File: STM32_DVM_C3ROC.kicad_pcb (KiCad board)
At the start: 4 copper layers, 65 x 56 mm, 18 parts, among them J3 40HAT, J6 CONN_02X02, J9 CONN_01X02, Q1 DMG2305UX, Q2 DMMT5401, U2 CAT24C32

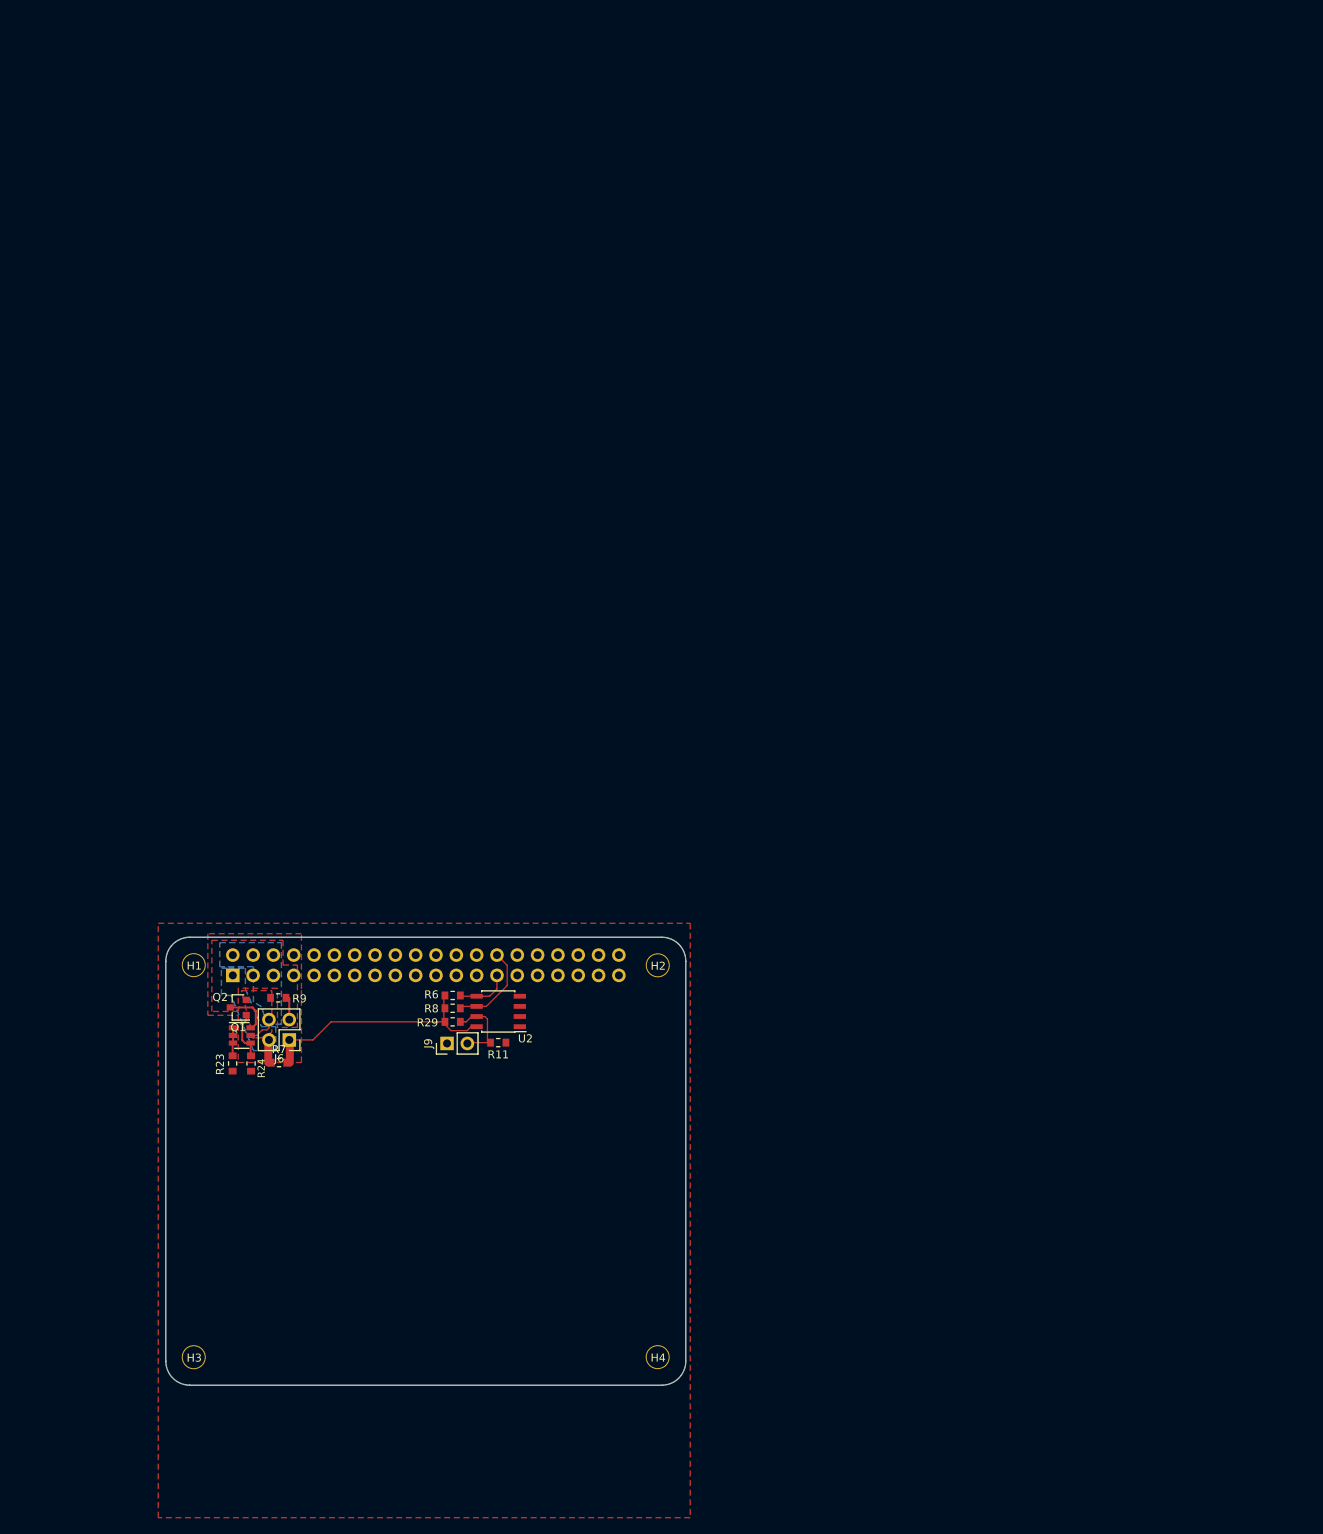
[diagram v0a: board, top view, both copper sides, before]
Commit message: Schaltplan fertig, Footprints zugewiesen, PCB Beginn platzierung
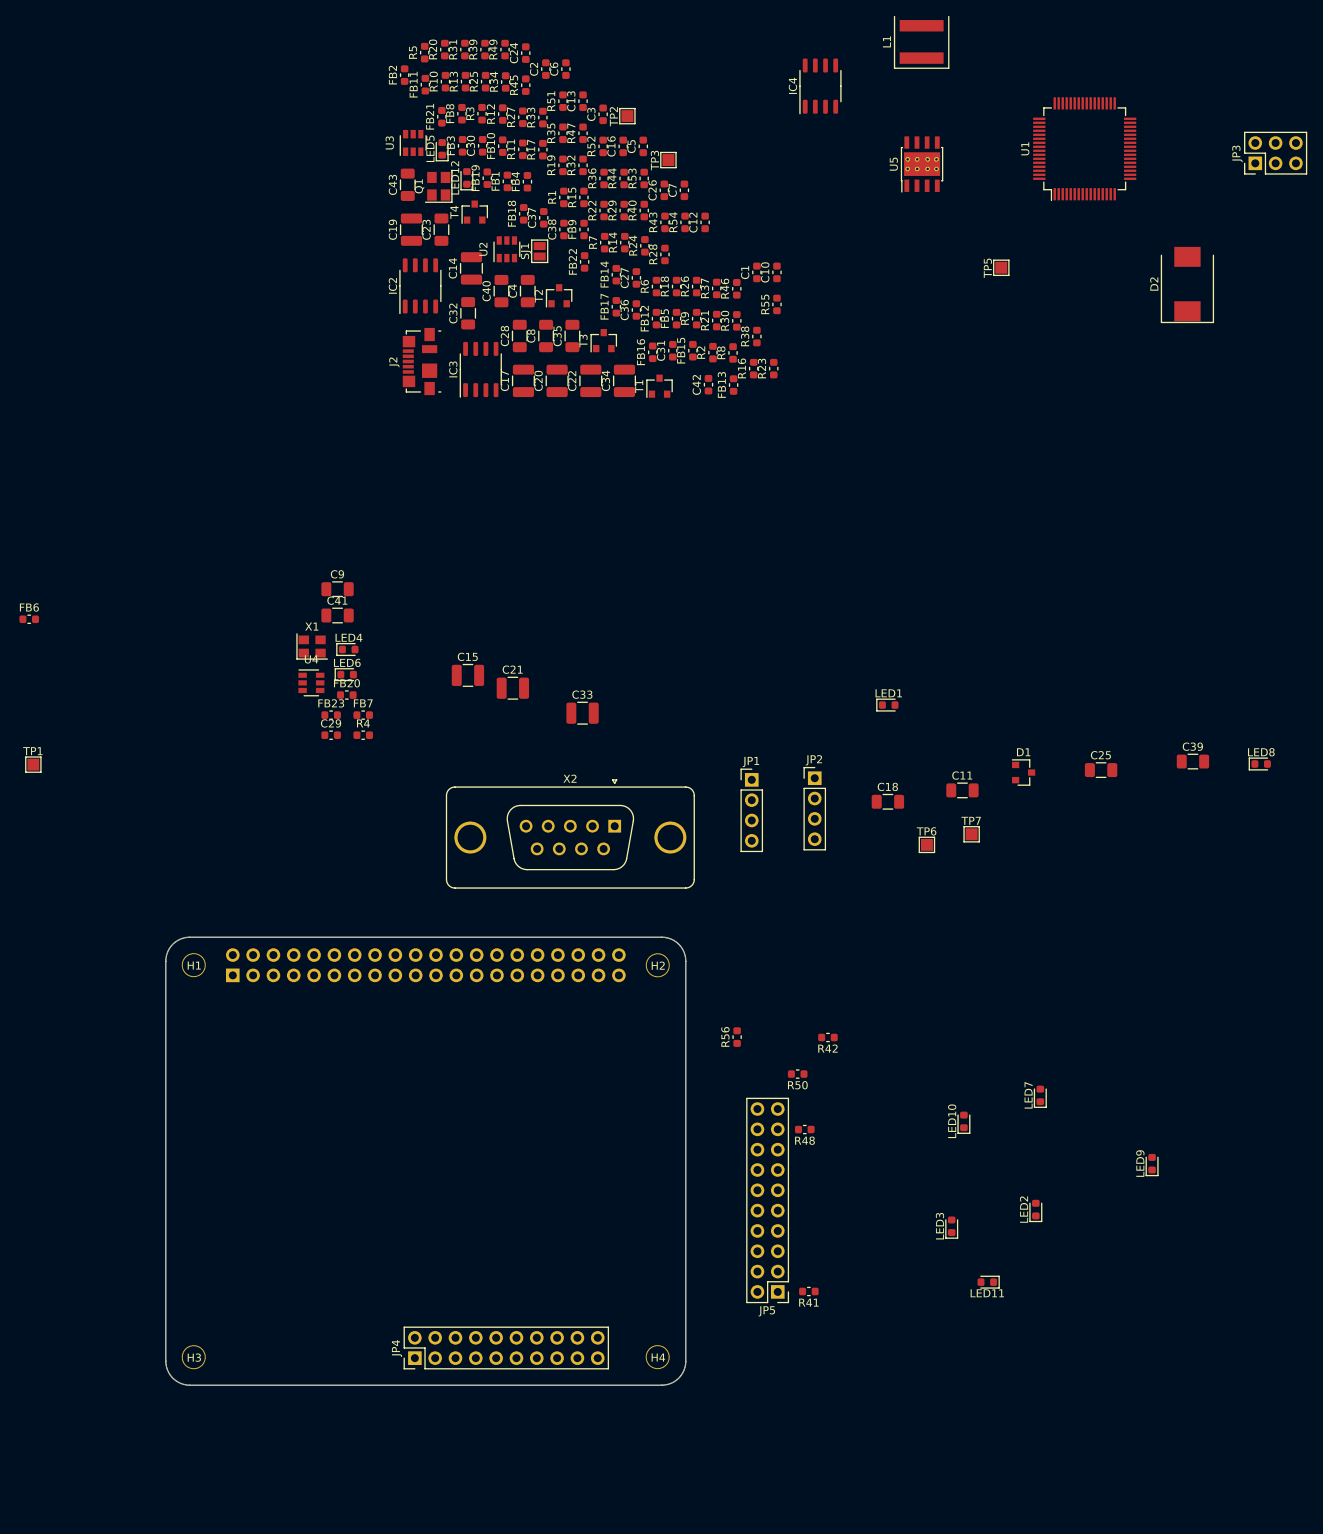
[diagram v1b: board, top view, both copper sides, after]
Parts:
- removed J6: CONN_02X02, Connector_PinHeader_2.54mm:PinHeader_2x02_P2.54mm_Vertical
- removed J9: CONN_01X02, Connector_PinHeader_2.54mm:PinHeader_1x02_P2.54mm_Vertical
- removed Q2: DMMT5401, Package_TO_SOT_SMD:SOT-23-6
- added C1: 100n, Capacitor_SMD:C_0603_1608Metric, F.Cu at (152.4, -22.3)
- added C10: 100n, Capacitor_SMD:C_0603_1608Metric, F.Cu at (154.9, -22.3)
- added C11: 4u7, Capacitor_SMD:C_1206_3216Metric, F.Cu at (178.1, 42.5)
- added C12: 10p, Capacitor_SMD:C_0603_1608Metric, F.Cu at (146.0, -28.5)
- added C13: 10p, Capacitor_SMD:C_0603_1608Metric, F.Cu at (130.7, -43.7)
- added C14: 22u, Capacitor_SMD:C_1210_3225Metric, F.Cu at (116.8, -22.8)
- added C15: 47u, Capacitor_SMD:C_1210_3225Metric, F.Cu at (116.3, 28.1)
- added C16: 100n, Capacitor_SMD:C_0603_1608Metric, F.Cu at (135.7, -38.0)
- added C17: 47u, Capacitor_SMD:C_1210_3225Metric, F.Cu at (123.3, -8.72)
- added C18: 4u7, Capacitor_SMD:C_1206_3216Metric, F.Cu at (168.8, 43.9)
- added C19: 22u, Capacitor_SMD:C_1210_3225Metric, F.Cu at (109.3, -27.6)
- added C2: 100n, Capacitor_SMD:C_0603_1608Metric, F.Cu at (126.1, -47.7)
- added C20: 22u, Capacitor_SMD:C_1210_3225Metric, F.Cu at (127.5, -8.72)
- added C21: 47u, Capacitor_SMD:C_1210_3225Metric, F.Cu at (121.9, 29.7)
- added C22: 47u, Capacitor_SMD:C_1210_3225Metric, F.Cu at (131.7, -8.72)
- added C23: 2u2, Capacitor_SMD:C_1206_3216Metric, F.Cu at (113.0, -27.6)
- added C24: 10n, Capacitor_SMD:C_0603_1608Metric, F.Cu at (123.5, -49.7)
- added C25: 2u2, Capacitor_SMD:C_1206_3216Metric, F.Cu at (195.5, 39.9)
- added C26: 10n, Capacitor_SMD:C_0603_1608Metric, F.Cu at (140.9, -32.5)
- added C27: 10n, Capacitor_SMD:C_0603_1608Metric, F.Cu at (137.4, -21.6)
- added C28: 4u7, Capacitor_SMD:C_1206_3216Metric, F.Cu at (122.8, -14.3)
- added C29: 680p, Capacitor_SMD:C_0603_1608Metric, F.Cu at (99.2, 35.6)
- added C3: 100n, Capacitor_SMD:C_0603_1608Metric, F.Cu at (133.2, -42.0)
- added C30: 10n, Capacitor_SMD:C_0603_1608Metric, F.Cu at (118.2, -38.1)
- added C31: 680p, Capacitor_SMD:C_0603_1608Metric, F.Cu at (141.9, -12.5)
- added C32: 4u7, Capacitor_SMD:C_1206_3216Metric, F.Cu at (116.3, -17.2)
- added C33: 22u, Capacitor_SMD:C_1210_3225Metric, F.Cu at (130.6, 32.8)
- added C34: 22u, Capacitor_SMD:C_1210_3225Metric, F.Cu at (135.9, -8.72)
- added C35: 4u7, Capacitor_SMD:C_1206_3216Metric, F.Cu at (129.4, -14.3)
- added C36: 6n8, Capacitor_SMD:C_0603_1608Metric, F.Cu at (137.4, -17.6)
- added C37: 47p, Capacitor_SMD:C_0603_1608Metric, F.Cu at (125.8, -29.1)
- added C38: 100n, Capacitor_SMD:C_0603_1608Metric, F.Cu at (128.3, -27.6)
- added C39: 22u, Capacitor_SMD:C_1206_3216Metric, F.Cu at (206.9, 38.9)
- added C4: 4u7, Capacitor_SMD:C_1206_3216Metric, F.Cu at (123.8, -19.9)
- added C40: 22u, Capacitor_SMD:C_1206_3216Metric, F.Cu at (120.5, -19.9)
- added C41: 1u, Capacitor_SMD:C_1206_3216Metric, F.Cu at (100.0, 20.6)
- added C42: 10n, Capacitor_SMD:C_0603_1608Metric, F.Cu at (146.4, -8.24)
- added C43: 1u, Capacitor_SMD:C_1206_3216Metric, F.Cu at (108.8, -33.2)
- added C5: 100n, Capacitor_SMD:C_0603_1608Metric, F.Cu at (138.2, -38.0)
- added C6: 100n, Capacitor_SMD:C_0603_1608Metric, F.Cu at (128.6, -47.7)
- added C7: 100n, Capacitor_SMD:C_0603_1608Metric, F.Cu at (143.4, -32.5)
- added C8: 4u7, Capacitor_SMD:C_1206_3216Metric, F.Cu at (126.1, -14.3)
- added C9: 4u7, Capacitor_SMD:C_1206_3216Metric, F.Cu at (100.0, 17.3)
- added D1: BAV70, Package_TO_SOT_SMD:SOT-23, F.Cu at (185.8, 40.2)
- added D2: B560C, Diode_SMD:D_SMC, F.Cu at (206.2, -20.8)
- added FB1: 100, Inductor_SMD:L_0603_1608Metric, F.Cu at (121.2, -33.7)
- added FB10: 100, Inductor_SMD:L_0603_1608Metric, F.Cu at (120.7, -38.1)
- added FB11: 100, Inductor_SMD:L_0603_1608Metric, F.Cu at (111.0, -45.7)
- added FB12: 100, Inductor_SMD:L_0603_1608Metric, F.Cu at (139.9, -16.5)
- added FB13: 100, Inductor_SMD:L_0603_1608Metric, F.Cu at (149.5, -8.20)
- added FB14: 100, Inductor_SMD:L_0603_1608Metric, F.Cu at (134.9, -22.0)
- added FB15: 100, Inductor_SMD:L_0603_1608Metric, F.Cu at (144.4, -12.5)
- added FB16: 100, Inductor_SMD:L_0603_1608Metric, F.Cu at (139.4, -12.3)
- added FB17: 100, Inductor_SMD:L_0603_1608Metric, F.Cu at (134.9, -18.0)
- added FB18: 100, Inductor_SMD:L_0603_1608Metric, F.Cu at (123.3, -29.6)
- added FB19: 100, Inductor_SMD:L_0603_1608Metric, F.Cu at (118.7, -34.1)
- added FB2: 100, Inductor_SMD:L_0603_1608Metric, F.Cu at (108.4, -46.9)
- added FB20: 100, Inductor_SMD:L_0603_1608Metric, F.Cu at (101.2, 30.5)
- added FB21: 100, Inductor_SMD:L_0603_1608Metric, F.Cu at (113.1, -41.7)
- added FB22: 100, Inductor_SMD:L_0603_1608Metric, F.Cu at (130.9, -23.6)
- added FB23: 100, Inductor_SMD:L_0603_1608Metric, F.Cu at (99.2, 33.1)
- added FB3: 100, Inductor_SMD:L_0603_1608Metric, F.Cu at (115.6, -38.1)
- added FB4: 100, Inductor_SMD:L_0603_1608Metric, F.Cu at (123.8, -33.6)
- added FB5: 100, Inductor_SMD:L_0603_1608Metric, F.Cu at (142.4, -16.5)
- added FB6: 100, Inductor_SMD:L_0603_1608Metric, F.Cu at (61.5, 21.1)
- added FB7: 100, Inductor_SMD:L_0603_1608Metric, F.Cu at (103.2, 33.1)
- added FB8: 100, Inductor_SMD:L_0603_1608Metric, F.Cu at (115.6, -42.1)
- added FB9: 100, Inductor_SMD:L_0603_1608Metric, F.Cu at (130.8, -27.6)
- added IC2: MCP6002, Package_SO:SO-8_3.9x4.9mm_P1.27mm, F.Cu at (110.4, -20.6)
- added IC3: MCP6002, Package_SO:SO-8_3.9x4.9mm_P1.27mm, F.Cu at (117.9, -10.1)
- added IC4: MCP6002, Package_SO:SO-8_3.9x4.9mm_P1.27mm, F.Cu at (160.4, -45.6)
- added J2: USB_B_Micro, Connector_USB:USB_Micro-B_Molex_47346-0001, F.Cu at (110.3, -11.1)
- added JP1: I2C Display, Connector_PinHeader_2.54mm:PinHeader_1x04_P2.54mm_Vertical, F.Cu at (151.8, 41.1)
- added JP2: Nextion Display, Connector_PinHeader_2.54mm:PinHeader_1x04_P2.54mm_Vertical, F.Cu at (159.7, 40.9)
- added JP3: Debug, Connector_PinHeader_2.54mm:PinHeader_2x03_P2.54mm_Vertical, F.Cu at (214.7, -35.9)
- added JP4: To LED + Display, Connector_PinHeader_2.54mm:PinHeader_2x10_P2.54mm_Vertical, F.Cu at (109.7, 113.4)
- added JP5: To STM32 DVM, Connector_PinHeader_2.54mm:PinHeader_2x10_P2.54mm_Vertical, F.Cu at (155.0, 105.2)
- added L1: 8u2, Inductor_SMD:L_Coilcraft_XAL60xx_6.36x6.56mm, F.Cu at (173.0, -51.1)
- added LED1: RED, LED_SMD:LED_0603_1608Metric, F.Cu at (168.9, 31.8)
- added LED10: YEL, LED_SMD:LED_0603_1608Metric, F.Cu at (178.3, 83.8)
- added LED11: YEL, LED_SMD:LED_0603_1608Metric, F.Cu at (181.2, 103.9)
- added LED12: VIO, LED_SMD:LED_0603_1608Metric, F.Cu at (116.2, -34.1)
- added LED2: BLU, LED_SMD:LED_0603_1608Metric, F.Cu at (187.3, 94.9)
- added LED3: ORG, LED_SMD:LED_0603_1608Metric, F.Cu at (176.8, 97.0)
- added LED4: ORG, LED_SMD:LED_0603_1608Metric, F.Cu at (101.4, 24.9)
- added LED5: GRN, LED_SMD:LED_0603_1608Metric, F.Cu at (113.1, -37.7)
- added LED6: RED, LED_SMD:LED_0603_1608Metric, F.Cu at (101.2, 28.0)
- added LED7: YEL, LED_SMD:LED_0603_1608Metric, F.Cu at (187.9, 80.6)
- added LED8: YEL, LED_SMD:LED_0603_1608Metric, F.Cu at (215.5, 39.2)
- added LED9: YEL, LED_SMD:LED_0603_1608Metric, F.Cu at (201.8, 89.1)
- added R1: 1k, Resistor_SMD:R_0603_1608Metric, F.Cu at (128.3, -31.7)
- added R10: 10K, Resistor_SMD:R_0603_1608Metric, F.Cu at (113.5, -46.1)
- added R12: 22k, Resistor_SMD:R_0603_1608Metric, F.Cu at (120.7, -42.1)
- added R13: 22k, Resistor_SMD:R_0603_1608Metric, F.Cu at (116.0, -46.1)
- added R14: 22k, Resistor_SMD:R_0603_1608Metric, F.Cu at (135.9, -26.0)
- added R15: 100k, Resistor_SMD:R_0603_1608Metric, F.Cu at (130.8, -31.7)
- added R16: 100k, Resistor_SMD:R_0603_1608Metric, F.Cu at (152.0, -10.3)
- added R17: 10K, Resistor_SMD:R_0603_1608Metric, F.Cu at (125.7, -37.6)
- added R18: 10k, Resistor_SMD:R_0603_1608Metric, F.Cu at (142.4, -20.5)
- added R19: 10k, Resistor_SMD:R_0603_1608Metric, F.Cu at (128.2, -35.7)
- added R2: 1k, Resistor_SMD:R_0603_1608Metric, F.Cu at (146.9, -12.3)
- added R20: 68k, Resistor_SMD:R_0603_1608Metric, F.Cu at (113.4, -50.1)
- added R21: 100k, Resistor_SMD:R_0603_1608Metric, F.Cu at (147.4, -16.3)
- added R22: 3k3, Resistor_SMD:R_0603_1608Metric, F.Cu at (133.3, -30.0)
- added R25: 3k3, Resistor_SMD:R_0603_1608Metric, F.Cu at (118.5, -46.1)
- added R26: 3k9, Resistor_SMD:R_0603_1608Metric, F.Cu at (144.9, -20.5)
- added R27: 39k, Resistor_SMD:R_0603_1608Metric, F.Cu at (123.2, -41.7)
- added R28: 3k9, Resistor_SMD:R_0603_1608Metric, F.Cu at (140.9, -24.5)
- added R3: 10K, Resistor_SMD:R_0603_1608Metric, F.Cu at (118.1, -42.1)
- added R30: 47k, Resistor_SMD:R_0603_1608Metric, F.Cu at (149.9, -16.2)
- added R31: 47, Resistor_SMD:R_0603_1608Metric, F.Cu at (115.9, -50.1)
- added R32: 10k, Resistor_SMD:R_0603_1608Metric, F.Cu at (130.7, -35.7)
- added R33: 10k, Resistor_SMD:R_0603_1608Metric, F.Cu at (125.7, -41.6)
- added R34: 1k, Resistor_SMD:R_0603_1608Metric, F.Cu at (121.0, -46.1)
- added R35: 10k, Resistor_SMD:R_0603_1608Metric, F.Cu at (128.2, -39.7)
- added R36: 1k, Resistor_SMD:R_0603_1608Metric, F.Cu at (133.3, -34.0)
- added R37: 47, Resistor_SMD:R_0603_1608Metric, F.Cu at (147.4, -20.3)
- added R38: 47k, Resistor_SMD:R_0603_1608Metric, F.Cu at (152.4, -14.3)
- added R39: 4k7, Resistor_SMD:R_0603_1608Metric, F.Cu at (118.4, -50.1)
- added R4: 10K, Resistor_SMD:R_0603_1608Metric, F.Cu at (103.2, 35.6)
- added R40: 10k, Resistor_SMD:R_0603_1608Metric, F.Cu at (138.4, -30.0)
- added R41: 1k, Resistor_SMD:R_0603_1608Metric, F.Cu at (158.9, 105.1)
- added R42: 560, Resistor_SMD:R_0603_1608Metric, F.Cu at (161.3, 73.4)
- added R43: 560, Resistor_SMD:R_0603_1608Metric, F.Cu at (140.9, -28.5)
- added R44: 560, Resistor_SMD:R_0603_1608Metric, F.Cu at (135.8, -34.0)
- added R45: 560, Resistor_SMD:R_0603_1608Metric, F.Cu at (123.5, -45.7)
- added R46: 560, Resistor_SMD:R_0603_1608Metric, F.Cu at (149.9, -20.2)
- added R47: 560, Resistor_SMD:R_0603_1608Metric, F.Cu at (130.7, -39.7)
- added R48: 560, Resistor_SMD:R_0603_1608Metric, F.Cu at (158.4, 84.9)
- added R49: 560, Resistor_SMD:R_0603_1608Metric, F.Cu at (121.0, -50.1)
- added R5: 10k, Resistor_SMD:R_0603_1608Metric, F.Cu at (110.9, -49.8)
- added R50: 560, Resistor_SMD:R_0603_1608Metric, F.Cu at (157.5, 77.9)
- added R51: 100k, Resistor_SMD:R_0603_1608Metric, F.Cu at (128.2, -43.7)
- added R52: 162k, Resistor_SMD:R_0603_1608Metric, F.Cu at (133.2, -38.0)
- added R53: 10k2, Resistor_SMD:R_0603_1608Metric, F.Cu at (138.3, -34.0)
- added R54: 53k6, Resistor_SMD:R_0603_1608Metric, F.Cu at (143.5, -28.5)
- added R55: 10k2, Resistor_SMD:R_0603_1608Metric, F.Cu at (154.9, -18.3)
- added R56: 560, Resistor_SMD:R_0603_1608Metric, F.Cu at (150.0, 73.3)
- added SJ1: Jumper_2_Open, Jumper:SolderJumper-2_P1.3mm_Open_Pad1.0x1.5mm, F.Cu at (125.3, -24.9)
- added T1: MMUN2214, Package_TO_SOT_SMD:SOT-23, F.Cu at (140.3, -8.06)
- added T2: MMUN2214, Package_TO_SOT_SMD:SOT-23, F.Cu at (127.7, -19.4)
- added T3: MMUN2214, Package_TO_SOT_SMD:SOT-23, F.Cu at (133.3, -13.8)
- added T4: MMUN2214, Package_TO_SOT_SMD:SOT-23, F.Cu at (117.2, -29.8)
- added TP1: TestPoint, TestPoint:TestPoint_Pad_1.5x1.5mm, F.Cu at (62.0, 39.2)
- added TP2: TestPoint, TestPoint:TestPoint_Pad_1.5x1.5mm, F.Cu at (136.2, -41.8)
- added TP3: RXA, TestPoint:TestPoint_Pad_1.5x1.5mm, F.Cu at (141.4, -36.3)
- added TP5: TestPoint, TestPoint:TestPoint_Pad_1.5x1.5mm, F.Cu at (183.0, -22.9)
- added TP6: TXA_R, TestPoint:TestPoint_Pad_1.5x1.5mm, F.Cu at (173.7, 49.3)
- added TP7: RSSI, TestPoint:TestPoint_Pad_1.5x1.5mm, F.Cu at (179.3, 48.0)
- added U1: STM32F446RETx, Package_QFP:LQFP-64_10x10mm_P0.5mm, F.Cu at (193.4, -37.7)
- added U3: USBLC6-2SC6, Package_TO_SOT_SMD:SOT-23-6, F.Cu at (109.5, -38.5)
- added U4: USBLC6-2SC6, Package_TO_SOT_SMD:SOT-23-6, F.Cu at (96.7, 29.0)
- added U5: TPS54360DDA, Package_SO:TI_SO-PowerPAD-8_ThermalVias, F.Cu at (173.1, -35.8)
- added X1: ASE-12MHz, Oscillator:Oscillator_SMD_Abracon_ASE-4Pin_3.2x2.5mm, F.Cu at (96.8, 24.5)
- added X2: To Radio, Connector_Dsub:DSUB-9_Female_Vertical_P2.77x2.84mm_MountingHoles, F.Cu at (134.7, 46.9)
- H1, H2, H3, H4: value 3mm_Mounting_Hole -> 3mm
- Q1: value DMG2305UX -> Crystal_GND23; footprint Package_TO_SOT_SMD:SOT-23 -> Crystal:Crystal_SMD_3225-4Pin_3.2x2.5mm
- R11: value DNP -> 22k; footprint Resistor_SMD:R_0603_1608Metric_Pad0.84x1.00mm_HandSolder -> Resistor_SMD:R_0603_1608Metric
- R23: value 10K -> 100k; footprint Resistor_SMD:R_0603_1608Metric_Pad0.84x1.00mm_HandSolder -> Resistor_SMD:R_0603_1608Metric
- R24: value 47K -> 39k; footprint Resistor_SMD:R_0603_1608Metric_Pad0.84x1.00mm_HandSolder -> Resistor_SMD:R_0603_1608Metric
- R29: value 10K -> 47; footprint Resistor_SMD:R_0603_1608Metric_Pad0.84x1.00mm_HandSolder -> Resistor_SMD:R_0603_1608Metric
- R6: value 3.9K -> 100k; footprint Resistor_SMD:R_0603_1608Metric_Pad0.84x1.00mm_HandSolder -> Resistor_SMD:R_0603_1608Metric
- R7: value DNP -> 100; footprint Resistor_SMD:R_0603_1608Metric_Pad0.84x1.00mm_HandSolder -> Resistor_SMD:R_0603_1608Metric
- R8: value 3.9K -> 10k; footprint Resistor_SMD:R_0603_1608Metric_Pad0.84x1.00mm_HandSolder -> Resistor_SMD:R_0603_1608Metric
- R9: value DNP -> 47; footprint Resistor_SMD:R_0603_1608Metric_Pad0.84x1.00mm_HandSolder -> Resistor_SMD:R_0603_1608Metric
- U2: value CAT24C32 -> USBLC6-2SC6; footprint Package_SOIC:SOIC-8_3.9x4.9mm_P1.27mm -> Package_TO_SOT_SMD:SOT-23-6
- moved R24 113.4 mm to (138.4, -25.6), turned to 90 degrees
- moved R11 111.7 mm to (123.2, -37.7), turned to 90 degrees
- moved R7 110.3 mm to (133.4, -26.0), turned to 90 degrees
- moved R23 110.1 mm to (154.5, -10.3), turned to 90 degrees
- moved Q1 105.7 mm to (112.7, -33.1), turned to 90 degrees
- moved R29 103.7 mm to (135.8, -30.0), turned to 90 degrees
- moved R9 99.7 mm to (144.9, -16.5), turned to 90 degrees
- moved U2 95.3 mm to (121.2, -25.2), turned to 90 degrees
- moved R6 92.2 mm to (139.9, -20.5), turned to 90 degrees
- moved R8 89.1 mm to (149.5, -12.2), turned to 90 degrees
- renumbered J3 to J1
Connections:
- J1 pad 1: /P3V3_HAT -> +3V3
- J1 pad 10: (no net) -> TXD_HOST
- J1 pad 11: (no net) -> Net-(J1-Pad11)
- J1 pad 12: (no net) -> Net-(J1-Pad12)
- J1 pad 13: (no net) -> Net-(J1-Pad13)
- J1 pad 14: GND -> INHIBIT
- J1 pad 15: (no net) -> Net-(J1-Pad15)
- J1 pad 16: (no net) -> Net-(J1-Pad16)
- J1 pad 17: (no net) -> +3V3
- J1 pad 18: (no net) -> Net-(J1-Pad18)
- J1 pad 19: (no net) -> Net-(J1-Pad19)
- J1 pad 2: /P5V_HAT -> +5V
- J1 pad 20: GND -> INHIBIT
- J1 pad 21: (no net) -> Net-(J1-Pad21)
- J1 pad 22: (no net) -> Net-(J1-Pad22)
- J1 pad 23: (no net) -> Net-(J1-Pad23)
- J1 pad 24: (no net) -> Net-(J1-Pad24)
- J1 pad 25: GND -> INHIBIT
- J1 pad 26: (no net) -> Net-(J1-Pad26)
- J1 pad 27: /ID_SD_EEPROM -> Net-(J1-Pad27)
- J1 pad 28: /ID_SC_EEPROM -> Net-(J1-Pad28)
- J1 pad 29: (no net) -> Net-(J1-Pad29)
- J1 pad 3: (no net) -> SDA
- J1 pad 30: GND -> INHIBIT
- J1 pad 31: (no net) -> Net-(J1-Pad31)
- J1 pad 32: (no net) -> Net-(J1-Pad32)
- J1 pad 33: (no net) -> Net-(J1-Pad33)
- J1 pad 34: GND -> INHIBIT
- J1 pad 35: (no net) -> Net-(J1-Pad35)
- J1 pad 36: (no net) -> Net-(J1-Pad36)
- J1 pad 37: (no net) -> Net-(J1-Pad37)
- J1 pad 38: (no net) -> Net-(J1-Pad38)
- J1 pad 39: GND -> INHIBIT
- J1 pad 4: /P5V_HAT -> +5V
- J1 pad 40: (no net) -> Net-(J1-Pad40)
- J1 pad 5: (no net) -> SCL
- J1 pad 6: GND -> INHIBIT
- J1 pad 7: (no net) -> Net-(J1-Pad7)
- J1 pad 8: (no net) -> RXD_HOST
- J1 pad 9: GND -> INHIBIT
- Q1 pad 1: Net-(Q1-Pad1) -> Net-(C12-Pad1)
- Q1 pad 2: /P5V_HAT -> INHIBIT
- Q1 pad 3: /P5V -> INHIBIT
- R11 pad 1: Net-(J9-Pad2) -> +5V
- R11 pad 2: GND -> Net-(C15-Pad1)
- R23 pad 2: GND -> Net-(IC3-Pad2)
- R24 pad 1: Net-(Q1-Pad1) -> Net-(C24-Pad1)
- R24 pad 2: GND -> Net-(C27-Pad1)
- R29 pad 1: /P3V3 -> +5V
- R29 pad 2: Net-(J9-Pad2) -> Net-(C28-Pad1)
- R6 pad 1: /P3V3 -> Net-(R6-Pad1)
- R6 pad 2: /ID_SD_EEPROM -> Net-(R10-Pad1)
- R7 pad 1: /P3V3_HAT -> Net-(R6-Pad1)
- R7 pad 2: /P3V3 -> INHIBIT
- R8 pad 1: /P3V3 -> TXA
- R8 pad 2: /ID_SC_EEPROM -> INHIBIT
- R9 pad 1: /P5V_HAT -> +3V3
- R9 pad 2: /P5V -> Net-(C18-Pad1)
- U2 pad 1: GND -> USB_D-
- U2 pad 2: GND -> INHIBIT
- U2 pad 3: GND -> USB_D+
- U2 pad 4: GND -> Net-(J2-Pad3)
- U2 pad 5: /ID_SD_EEPROM -> Net-(J2-Pad1)
- U2 pad 6: /ID_SC_EEPROM -> Net-(J2-Pad2)
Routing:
- net /P3V3: track 31.3 -> 0.00 mm
- net /ID_SC_EEPROM: track 11.7 -> 0.00 mm
- net Net-(J9-Pad2): track 9.58 -> 0.00 mm
- net /P5V: track 8.71 -> 0.00 mm
- net /ID_SD_EEPROM: track 7.43 -> 0.00 mm
- net Net-(Q1-Pad1): track 6.02 -> 0.00 mm
- net /P5V_HAT: track 3.77 -> 0.00 mm
- net Net-(IC3-Pad1): track 3.37 -> 0.00 mm
- net /P3V3_HAT: track 2.88 -> 0.00 mm
- added copper zone on In2.Cu, net INHIBIT
- removed copper zone on B.Cu, net /P3V3_HAT
- removed copper zone on F.Cu, net /P5V
- removed copper zone on B.Cu, net /P5V_HAT
- removed copper zone on F.Cu, net /P5V_HAT
- removed copper zone on F.Cu, net GND
- removed copper zone on In2.Cu, net GND
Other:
- board text removed: "If you want to use an SMT 40-pin header, please move the top edge up by 0.5mm and locate the header in the same location as the current TH part."
- board text removed: "This is a HAT compatible PCB starting design based on the official Raspberry Pi specs at: https://github.com/raspberrypi/hats/blob/master/designguide.md Currently the camera slot and display cutout are not here. See the schematic for the details on the EEPROM and power setup. This board does have the correct components for powering the Pi via the HAT. If you need the Pi to provide 5V or 3.3V, ple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"
